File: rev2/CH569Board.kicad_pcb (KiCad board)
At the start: 4 copper layers, 47.3 x 49.6 mm, 41 parts, among them CN1 BA42-80BT-1-NHB, J1 Conn_01x02_Male, J2 Conn_01x03_Male, SW1 TS-1187A-B-A-B, U1 SPX3819M5-L-3-3/TR, U4 CH569W, X1 X1E0000210295

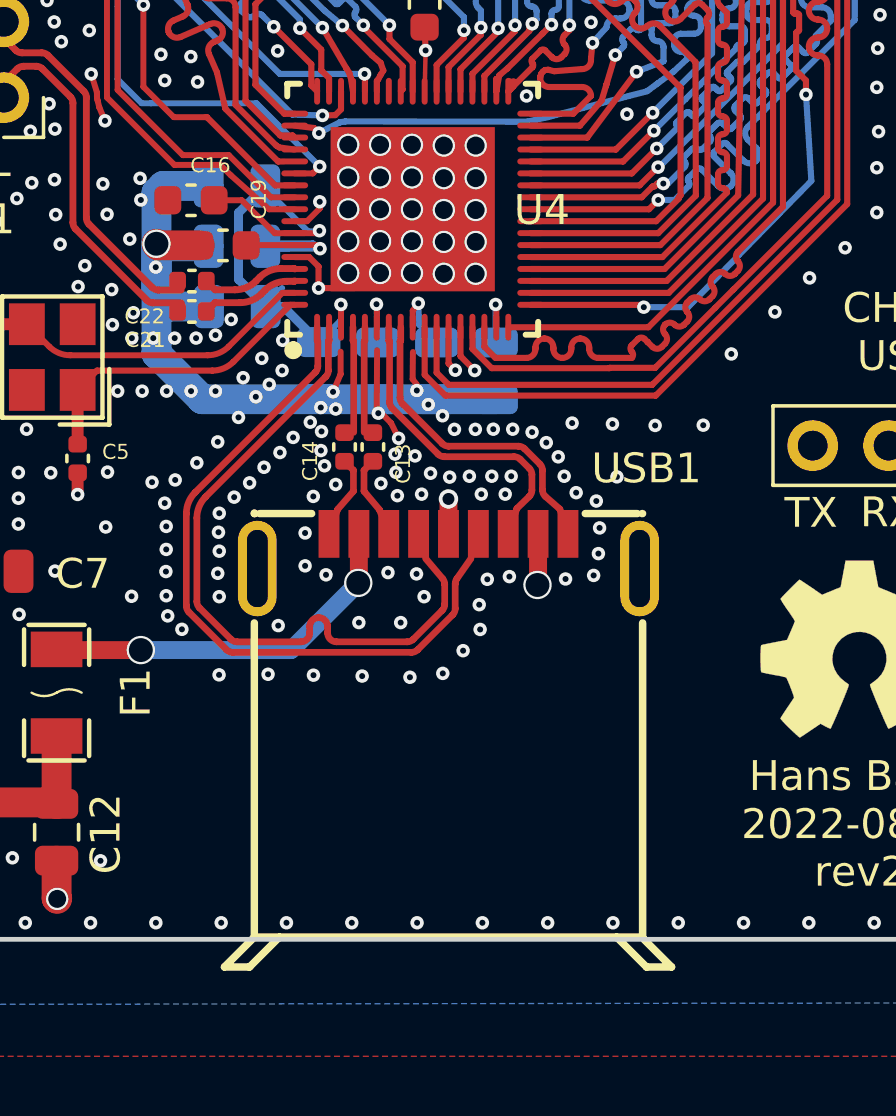
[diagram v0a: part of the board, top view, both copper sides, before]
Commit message: fix Pin64 short to ground and missing decoupling cap connection
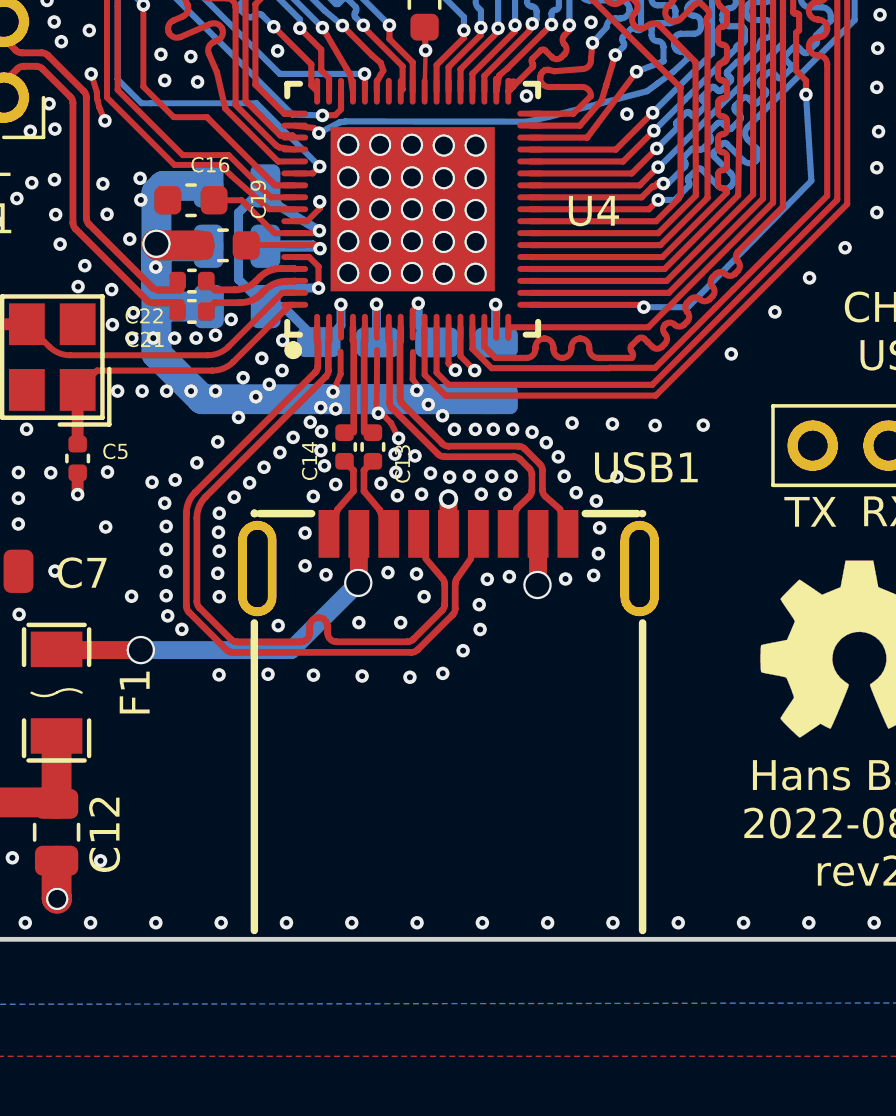
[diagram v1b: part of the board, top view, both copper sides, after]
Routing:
- net +1V2: track 18.5 -> 19.3 mm
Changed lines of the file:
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@@
       (effects (font (size 1 1) (thickness 0.15)))
     )
-    (fp_line (start 6.47 12.92) (end 7.47 13.92) (layer "F.SilkS") (width 0.25))
-    (fp_line (start 7.47 13.92) (end 6.63 13.92) (layer "F.SilkS") (width 0.25))
-    (fp_line (start -6.5 12.92) (end 6.5 12.92) (layer "F.SilkS") (width 0.25))
-    (fp_line (start -7.5 13.92) (end -6.66 13.92) (layer "F.SilkS") (width 0.25))
-    (fp_line (start 6.5 12.92) (end 6.5 2.4) (layer "F.SilkS") (width 0.25))
+    (fp_line (start 6.5 12.7) (end 6.5 2.4) (layer "F.SilkS") (width 0.25))
     (fp_line (start -6.5 -1.26) (end -6.5 -1.28) (layer "F.SilkS") (width 0.25))
-    (fp_line (start -6.5 12.92) (end -7.5 13.92) (layer "F.SilkS") (width 0.25))
     (fp_line (start -6.32 -1.26) (end -4.58 -1.26) (layer "F.SilkS") (width 0.25))
-    (fp_line (start -6.66 13.92) (end -5.66 12.92) (layer "F.SilkS") (width 0.25))
     (fp_line (start -6.5 -1.26) (end -6.48 -1.26) (layer "F.SilkS") (width 0.25))
-    (fp_line (start -6.5 12.92) (end -6.5 2.4) (layer "F.SilkS") (width 0.25))
+    (fp_line (start -6.5 12.7) (end -6.5 2.4) (layer "F.SilkS") (width 0.25))
     (fp_line (start 4.58 -1.26) (end 6.32 -1.26) (layer "F.SilkS") (width 0.25))
     (fp_line (start 6.48 -1.26) (end 6.5 -1.26) (layer "F.SilkS") (width 0.25))
-    (fp_line (start 6.63 13.92) (end 5.63 12.92) (layer "F.SilkS") (width 0.25))
     (fp_circle (center -6.55 -1.23) (end -6.52 -1.23) (layer "F.Fab") (width 0.06) (fill none))
-    (pad "1" smd rect locked (at -3 -0.58) (size 0.7 1.6) (layers "F.Cu" "F.Paste" "F.Mask")
+    (pad "1" smd rect (at -3 -0.58) (size 0.7 1.6) (layers "F.Cu" "F.Paste" "F.Mask")
       (net 80 "/VBUS") (pinfunction "VBUS") (pintype "unspecified"))
-    (pad "2" smd rect locked (at -1 -0.58) (size 0.7 1.6) (layers "F.Cu" "F.Paste" "F.Mask")
+    (pad "2" smd rect (at -1 -0.58) (size 0.7 1.6) (layers "F.Cu" "F.Paste" "F.Mask")
       (net 67 "/D-") (pinfunction "D-") (pintype "unspecified"))
-    (pad "3" smd rect locked (at 1 -0.58) (size 0.7 1.6) (layers "F.Cu" "F.Paste" "F.Mask")
+    (pad "3" smd rect (at 1 -0.58) (size 0.7 1.6) (layers "F.Cu" "F.Paste" "F.Mask")
       (net 66 "/D+") (pinfunction "D+") (pintype "unspecified"))
-    (pad "4" smd rect locked (at 3 -0.58) (size 0.7 1.6) (layers "F.Cu" "F.Paste" "F.Mask")
+    (pad "4" smd rect (at 3 -0.58) (size 0.7 1.6) (layers "F.Cu" "F.Paste" "F.Mask")
       (net 1 "GND") (pinfunction "GND") (pintype "unspecified"))
-    (pad "5" smd rect locked (at 4 -0.58) (size 0.7 1.6) (layers "F.Cu" "F.Paste" "F.Mask")
+    (pad "5" smd rect (at 4 -0.58) (size 0.7 1.6) (layers "F.Cu" "F.Paste" "F.Mask")
       (net 69 "/SSRX-") (pinfunction "STDA_SSRX-") (pintype "unspecified"))
-    (pad "6" smd rect locked (at 2 -0.58) (size 0.7 1.6) (layers "F.Cu" "F.Paste" "F.Mask")
+    (pad "6" smd rect (at 2 -0.58) (size 0.7 1.6) (layers "F.Cu" "F.Paste" "F.Mask")
       (net 68 "/SSRX+") (pinfunction "STDA_SSRX+") (pintype "unspecified"))
-    (pad "7" smd rect locked (at 0 -0.58) (size 0.7 1.6) (layers "F.Cu" "F.Paste" "F.Mask")
+    (pad "7" smd rect (at 0 -0.58) (size 0.7 1.6) (layers "F.Cu" "F.Paste" "F.Mask")
       (net 1 "GND") (pinfunction "GND_DRAIN") (pintype "unspecified"))
-    (pad "8" smd rect locked (at -2 -0.58) (size 0.7 1.6) (layers "F.Cu" "F.Paste" "F.Mask")
+    (pad "8" smd rect (at -2 -0.58) (size 0.7 1.6) (layers "F.Cu" "F.Paste" "F.Mask")
       (net 78 "/STDA_SSTX-") (pinfunction "STDA_SSTX-") (pintype "unspecified"))
-    (pad "9" smd rect locked (at -4 -0.58) (size 0.7 1.6) (layers "F.Cu" "F.Paste" "F.Mask")
+    (pad "9" smd rect (at -4 -0.58) (size 0.7 1.6) (layers "F.Cu" "F.Paste" "F.Mask")
       (net 79 "/STDA_SSTX+") (pinfunction "STDA_SSTX+") (pintype "unspecified"))
-    (pad "10" thru_hole oval locked (at -6.4 0.58) (size 1.3 3.2) (drill oval 0.700024 2.599995) (layers *.Cu *.Paste *.Mask)
+    (pad "10" thru_hole oval (at -6.4 0.58) (size 1.3 3.2) (drill oval 0.700024 2.599995) (layers *.Cu *.Paste *.Mask)
       (net 20 "unconnected-(USB1-Pad10)") (pinfunction "10") (pintype "unspecified+no_connect"))
-    (pad "11" thru_hole oval locked (at 6.4 0.58 180) (size 1.3 3.2) (drill oval 0.700024 2.599995) (layers *.Cu *.Paste *.Mask)
+    (pad "11" thru_hole oval (at 6.4 0.58 180) (size 1.3 3.2) (drill oval 0.700024 2.599995) (layers *.Cu *.Paste *.Mask)
       (net 22 "unconnected-(USB1-Pad11)") (pinfunction "11") (pintype "unspecified+no_connect"))
     (model "/home/jack/Documents/Kicad/easyeda2kicad/easyeda2kicad.3dshapes/USB-A-SMD_U231-091N-4BLRA00-S-1.wrl"
@@
     (property "Sheetname" "")
     (attr through_hole)
-    (fp_text reference "U4" (at 4.3274 0.03) (layer "F.SilkS")
+    (fp_text reference "U4" (at 6.0474 0.09) (layer "F.SilkS")
       (effects (font (size 1 1) (thickness 0.15)))
     )
@@
   (segment (start 118.77 102.58) (end 117.25 102.58) (width 1) (layer "B.Cu") (net 1))
   (segment (start 117.46 106.62) (end 117.023147 106.183147) (width 1) (layer "B.Cu") (net 1))
-  (segment (start 122.45 106) (end 123.67 106) (width 0.20574) (layer "F.Cu") (net 2))
   (segment (start 104.539 109.471) (end 104.539 108.191) (width 1) (layer "F.Cu") (net 2))
   (segment (start 123.203 107.312) (end 123.203 106.553) (width 0.2) (layer "F.Cu") (net 2))
@@
   (segment (start 112.45 101.55) (end 118.58 101.53) (width 0.6) (layer "In2.Cu") (net 2))
   (segment (start 121.2 104.11) (end 118.62 101.53) (width 0.2) (layer "In2.Cu") (net 2))
-  (segment (start 122.11 104.11) (end 120.65 102.65) (width 0.2) (layer "B.Cu") (net 2))
+  (segment (start 128.38 107.8) (end 128.4 107.82) (width 0.3) (layer "B.Cu") (net 2))
   (segment (start 120.67 102.58) (end 119.77 103.48) (width 0.3) (layer "B.Cu") (net 2))
-  (segment (start 121.23 106) (end 120.68 106.55) (width 0.20574) (layer "B.Cu") (net 2))
+  (segment (start 123.2 107.25) (end 123.1 107.35) (width 0.3) (layer "B.Cu") (net 2))
+  (segment (start 121.15 106) (end 120.68 106.47) (width 0.20574) (layer "B.Cu") (net 2))
   (segment (start 121.27 106.62) (end 122.46 107.81) (width 0.3) (layer "B.Cu") (net 2))
-  (segment (start 128.38 107.8) (end 128.4 107.82) (width 0.2) (layer "B.Cu") (net 2))
-  (segment (start 123.2 107.07) (end 122.46 107.81) (width 0.2) (layer "B.Cu") (net 2))
+  (segment (start 120.68 106.47) (end 120.68 106.62) (width 0.20574) (layer "B.Cu") (net 2))
   (segment (start 119.77 105.71) (end 120.68 106.62) (width 0.3) (layer "B.Cu") (net 2))
+  (segment (start 122.45 106) (end 121.15 106) (width 0.3) (layer "B.Cu") (net 2))
+  (segment (start 121.125 103.25) (end 120.67 102.58) (width 0.3) (layer "B.Cu") (net 2))
   (segment (start 120.68 106.62) (end 121.27 106.62) (width 0.3) (layer "B.Cu") (net 2))
-  (segment (start 123.2 106.55) (end 123.2 107.07) (width 0.2) (layer "B.Cu") (net 2))
   (segment (start 119.77 103.48) (end 119.77 105.71) (width 0.3) (layer "B.Cu") (net 2))
-  (segment (start 122.48 104.08) (end 122.11 104.11) (width 0.2) (layer "B.Cu") (net 2))
-  (segment (start 128.38 106.55) (end 128.38 107.8) (width 0.2) (layer "B.Cu") (net 2))
+  (segment (start 123.1 107.35) (end 122.64 107.81) (width 0.2) (layer "B.Cu") (net 2))
+  (segment (start 122.48 104.08) (end 121.125 103.25) (width 0.3) (layer "B.Cu") (net 2))
+  (segment (start 128.38 106.55) (end 128.38 107.8) (width 0.3) (layer "B.Cu") (net 2))
+  (segment (start 122.64 107.81) (end 122.46 107.81) (width 0.2) (layer "B.Cu") (net 2))
+  (segment (start 123.2 106.55) (end 123.2 107.25) (width 0.3) (layer "B.Cu") (net 2))
   (segment (start 110.505 118.0474) (end 110.505 115.4824) (width 1) (layer "F.Cu") (net 3))
   (segment (start 106.8324 120.6652) (end 106.8324 118.0686) (width 1) (layer "F.Cu") (net 3))
@@
   (segment (start 122.5 104.68) (end 120.756503 104.686503) (width 0.2) (layer "B.Cu") (net 24))
   (segment (start 120.766959 104.503041) (end 120.67 104.6) (width 0.2) (layer "B.Cu") (net 24))
-  (segment (start 125.79 106.51) (end 125.82 107.23) (width 0.2) (layer "B.Cu") (net 24))
-  (segment (start 125.82 107.23) (end 126.41 107.82) (width 0.2) (layer "B.Cu") (net 24))
+  (segment (start 125.79 106.51) (end 125.79 107.2) (width 0.3) (layer "B.Cu") (net 24))
+  (segment (start 124.39 106.54) (end 124.39 107.78) (width 0.3) (layer "B.Cu") (net 24))
   (segment (start 122.33 104.57) (end 122.263041 104.503041) (width 0.2) (layer "B.Cu") (net 24))
-  (segment (start 124.4 106.56) (end 124.41 107.8) (width 0.2) (layer "B.Cu") (net 24))
+  (segment (start 124.39 107.78) (end 124.43 107.82) (width 0.3) (layer "B.Cu") (net 24))
+  (segment (start 125.79 107.2) (end 126.41 107.82) (width 0.3) (layer "B.Cu") (net 24))
   (segment (start 120.756503 104.686503) (end 120.67 104.6) (width 0.2) (layer "B.Cu") (net 24))
   (segment (start 122.263041 104.503041) (end 120.766959 104.503041) (width 0.2) (layer "B.Cu") (net 24))
+  (segment (start 125.8 107.35) (end 126.41 107.82) (width 0.2) (layer "B.Cu") (net 24))
   (segment (start 124.0026 107.76) (end 123.9786 107.784) (width 0.225) (layer "F.Cu") (net 25))
   (segment (start 123.9786 107.784) (end 123.9786 110.83) (width 0.225) (layer "F.Cu") (net 25))
